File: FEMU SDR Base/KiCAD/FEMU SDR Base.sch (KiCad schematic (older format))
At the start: 11 parts

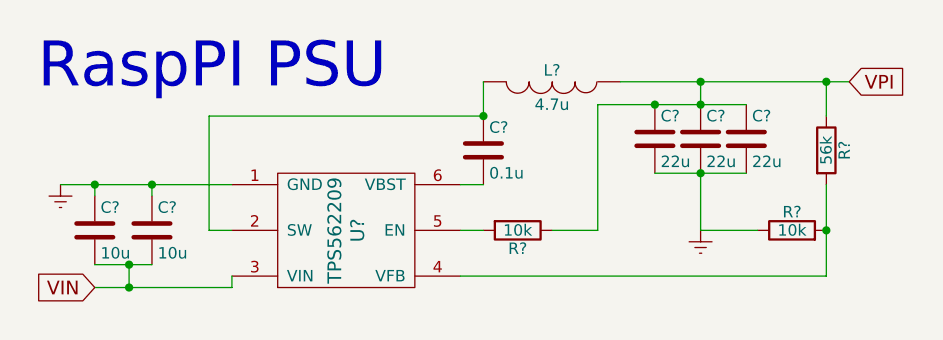
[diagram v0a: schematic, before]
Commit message: STATUS changed to FREE; Footprint ascociations added
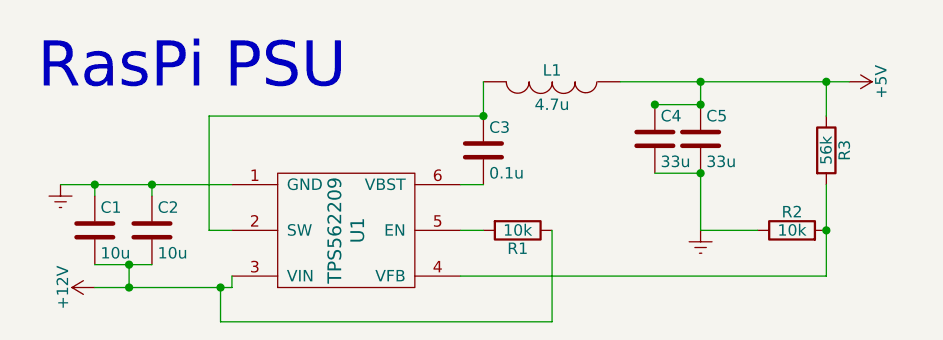
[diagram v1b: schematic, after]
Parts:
- removed C?: 22u, symbol C
- C4, C5: renamed from C?; value 22u -> 33u
- gave numbers to parts that had none: 8
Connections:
- net VIN renamed +12V
- net +12V: now also R1.1
- net VPI renamed +5V
- net +5V: no longer R1.1
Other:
- note added: "RasPi PSU"
- note removed: "RaspPI PSU"
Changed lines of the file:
@@
 LIBS:valves
 LIBS:ARB_lib
+LIBS:FEMU SDR Base-cache
 EELAYER 25 0
 EELAYER END
@@
 $EndDescr
 $Comp
-L TPS562209 U?
+L TPS562209 U1
 U 1 1 5703A8E6
 P 1800 1350
-F 0 "U?" V 1850 1350 60  0000 C CNN
+F 0 "U1" V 1850 1350 60  0000 C CNN
 F 1 "TPS562209" V 1750 1350 60  0000 C CNN
-F 2 "" H 1800 1250 60  0000 C CNN
+F 2 "" H 1800 1250 60  0001 C CNN
 F 3 "" H 1800 1250 60  0000 C CNN
 	1    1800 1350
@@
 $EndComp
 Text Notes 450  750  0    197  ~ 0
-RaspPI PSU
-$Comp
-L C C?
+RasPi PSU
+$Comp
+L C C1
 U 1 1 5703ADE8
 P 700 1350
-F 0 "C?" H 725 1450 50  0000 L CNN
+F 0 "C1" H 725 1450 50  0000 L CNN
 F 1 "10u" H 725 1250 50  0000 L CNN
-F 2 "" H 738 1200 50  0000 C CNN
+F 2 "" H 738 1200 50  0001 C CNN
 F 3 "" H 700 1350 50  0000 C CNN
 	1    700  1350
@@
 $EndComp
 $Comp
-L C C?
+L C C2
 U 1 1 5703AE4B
 P 950 1350
-F 0 "C?" H 975 1450 50  0000 L CNN
+F 0 "C2" H 975 1450 50  0000 L CNN
 F 1 "10u" H 975 1250 50  0000 L CNN
-F 2 "" H 988 1200 50  0000 C CNN
+F 2 "" H 988 1200 50  0001 C CNN
 F 3 "" H 950 1350 50  0000 C CNN
 	1    950  1350
 	1    0    0    -1
 $EndComp
-Text GLabel 700  1600 0    60   Input ~ 0
-VIN
-$Comp
-L Earth #PWR?
+$Comp
+L Earth #PWR01
 U 1 1 5703AF6B
 P 550 1150
-F 0 "#PWR?" H 550 900 50  0001 C CNN
+F 0 "#PWR01" H 550 900 50  0001 C CNN
 F 1 "Earth" H 550 1000 50  0001 C CNN
 F 2 "" H 550 1150 50  0000 C CNN
@@
 $EndComp
 $Comp
-L C C?
+L C C3
 U 1 1 5703B087
 P 2400 1000
-F 0 "C?" H 2425 1100 50  0000 L CNN
+F 0 "C3" H 2425 1100 50  0000 L CNN
 F 1 "0.1u" H 2425 900 50  0000 L CNN
-F 2 "" H 2438 850 50  0000 C CNN
+F 2 "" H 2438 850 50  0001 C CNN
 F 3 "" H 2400 1000 50  0000 C CNN
 	1    2400 1000
@@
 $EndComp
 $Comp
-L INDUCTOR L?
+L INDUCTOR L1
 U 1 1 5703B202
 P 2700 700
-F 0 "L?" V 2650 700 50  0000 C CNN
+F 0 "L1" V 2650 700 50  0000 C CNN
 F 1 "4.7u" V 2800 700 50  0000 C CNN
-F 2 "" H 2700 700 50  0000 C CNN
+F 2 "" H 2700 700 50  0001 C CNN
 F 3 "" H 2700 700 50  0000 C CNN
 	1    2700 700
@@
 $EndComp
 $Comp
-L R R?
+L R R1
 U 1 1 5703B2B6
 P 2550 1350
-F 0 "R?" V 2630 1350 50  0000 C CNN
+F 0 "R1" V 2630 1350 50  0000 C CNN
 F 1 "10k" V 2550 1350 50  0000 C CNN
-F 2 "" V 2480 1350 50  0000 C CNN
+F 2 "" V 2480 1350 50  0001 C CNN
 F 3 "" H 2550 1350 50  0000 C CNN
 	1    2550 1350
@@
 $EndComp
 $Comp
-L C C?
+L C C4
 U 1 1 5703B4E6
 P 3150 950
-F 0 "C?" H 3175 1050 50  0000 L CNN
-F 1 "22u" H 3175 850 50  0000 L CNN
-F 2 "" H 3188 800 50  0000 C CNN
+F 0 "C4" H 3175 1050 50  0000 L CNN
+F 1 "33u" H 3175 850 50  0000 L CNN
+F 2 "" H 3188 800 50  0001 C CNN
 F 3 "" H 3150 950 50  0000 C CNN
 	1    3150 950
@@
 $EndComp
 $Comp
-L C C?
+L C C5
 U 1 1 5703BAB5
 P 3350 950
-F 0 "C?" H 3375 1050 50  0000 L CNN
-F 1 "22u" H 3375 850 50  0000 L CNN
-F 2 "" H 3388 800 50  0000 C CNN
+F 0 "C5" H 3375 1050 50  0000 L CNN
+F 1 "33u" H 3375 850 50  0000 L CNN
+F 2 "" H 3388 800 50  0001 C CNN
 F 3 "" H 3350 950 50  0000 C CNN
 	1    3350 950
@@
 $EndComp
 $Comp
-L C C?
-U 1 1 5703BAE1
-P 3550 950
-F 0 "C?" H 3575 1050 50  0000 L CNN
-F 1 "22u" H 3575 850 50  0000 L CNN
-F 2 "" H 3588 800 50  0000 C CNN
-F 3 "" H 3550 950 50  0000 C CNN
-	1    3550 950
-	1    0    0    -1
-$EndComp
-Text GLabel 4000 700  2    60   Input ~ 0
-VPI
-$Comp
-L R R?
+L R R2
 U 1 1 5703C072
 P 3750 1350
-F 0 "R?" V 3830 1350 50  0000 C CNN
+F 0 "R2" V 3830 1350 50  0000 C CNN
 F 1 "10k" V 3750 1350 50  0000 C CNN
-F 2 "" V 3680 1350 50  0000 C CNN
+F 2 "" V 3680 1350 50  0001 C CNN
 F 3 "" H 3750 1350 50  0000 C CNN
 	1    3750 1350
@@
 $EndComp
 $Comp
-L R R?
+L R R3
 U 1 1 5703C16C
 P 3900 1000
-F 0 "R?" V 3980 1000 50  0000 C CNN
+F 0 "R3" V 3980 1000 50  0000 C CNN
 F 1 "56k" V 3900 1000 50  0000 C CNN
-F 2 "" V 3830 1000 50  0000 C CNN
+F 2 "" V 3830 1000 50  0001 C CNN
 F 3 "" H 3900 1000 50  0000 C CNN
 	1    3900 1000
@@
 $EndComp
 $Comp
-L Earth #PWR?
+L Earth #PWR02
 U 1 1 5703C400
 P 3350 1350
-F 0 "#PWR?" H 3350 1100 50  0001 C CNN
+F 0 "#PWR02" H 3350 1100 50  0001 C CNN
 F 1 "Earth" H 3350 1200 50  0001 C CNN
 F 2 "" H 3350 1350 50  0000 C CNN
@@
 Wire Wire Line
 	2400 850  2400 700
-Wire Wire Line
-	2400 1350 2300 1350
-Wire Wire Line
-	2900 800  3550 800
 Connection ~ 3350 800
 Wire Wire Line
 	3350 700  3350 800
-Wire Wire Line
-	2900 800  2900 1350
-Wire Wire Line
-	2900 1350 2700 1350
 Connection ~ 3150 800
 Connection ~ 3350 700
@@
 	3900 1550 2300 1550
 Connection ~ 3900 1350
-Wire Wire Line
-	3150 1100 3550 1100
 Connection ~ 3350 1100
 Wire Wire Line
@@
 Wire Wire Line
 	3350 1350 3600 1350
+Wire Wire Line
+	2400 1350 2300 1350
+Wire Wire Line
+	2700 1350 2700 1750
+Wire Wire Line
+	2700 1750 1250 1750
+Wire Wire Line
+	1250 1750 1250 1600
+Connection ~ 1250 1600
+Wire Wire Line
+	3350 800  3150 800
+Wire Wire Line
+	3350 1100 3150 1100
+$Comp
+L +12V #PWR03
+U 1 1 57077D61
+P 700 1600
+F 0 "#PWR03" H 700 1450 50  0001 C CNN
+F 1 "+12V" H 700 1740 50  0000 C CNN
+F 2 "" H 700 1600 50  0000 C CNN
+F 3 "" H 700 1600 50  0000 C CNN
+	1    700  1600
+	0    -1   -1   0
+$EndComp
+$Comp
+L +5V #PWR04
+U 1 1 57077E13
+P 4000 700
+F 0 "#PWR04" H 4000 550 50  0001 C CNN
+F 1 "+5V" H 4000 840 50  0000 C CNN
+F 2 "" H 4000 700 50  0000 C CNN
+F 3 "" H 4000 700 50  0000 C CNN
+	1    4000 700
+	0    1    1    0
+$EndComp
 $EndSCHEMATC

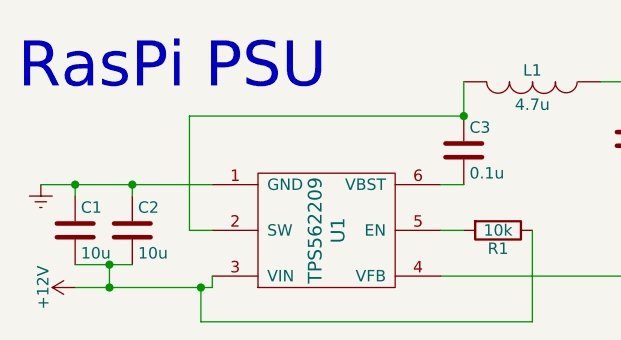
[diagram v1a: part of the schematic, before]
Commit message: STATUS = FREE ; pcbnew layout of RasPi PSU added, Changed to 4 layers.
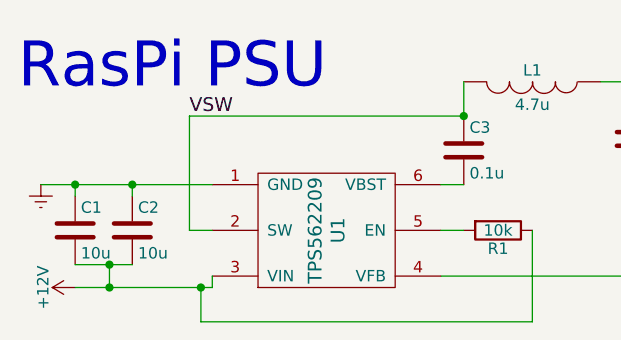
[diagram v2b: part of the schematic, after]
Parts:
- C1, C2, C3: footprint (none) -> Capacitors_SMD:C_0805_HandSoldering
- C4, C5: footprint (none) -> Capacitors_SMD:C_1206_HandSoldering
- L1: footprint (none) -> ARB_foots:L_Wurth_74404052039
- R1, R2, R3: footprint (none) -> Resistors_SMD:R_0805_HandSoldering
- U1: footprint (none) -> ARB_foots:TPS562209
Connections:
- net VSW: now reaches C3.1, L1.2, U1.2 (SW)
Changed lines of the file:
@@
 F 0 "U1" V 1850 1350 60  0000 C CNN
 F 1 "TPS562209" V 1750 1350 60  0000 C CNN
-F 2 "" H 1800 1250 60  0001 C CNN
+F 2 "ARB_foots:TPS562209" H 1800 1250 60  0001 C CNN
 F 3 "" H 1800 1250 60  0000 C CNN
 	1    1800 1350
@@
 F 0 "C1" H 725 1450 50  0000 L CNN
 F 1 "10u" H 725 1250 50  0000 L CNN
-F 2 "" H 738 1200 50  0001 C CNN
+F 2 "Capacitors_SMD:C_0805_HandSoldering" H 738 1200 50  0001 C CNN
 F 3 "" H 700 1350 50  0000 C CNN
 	1    700  1350
@@
 F 0 "C2" H 975 1450 50  0000 L CNN
 F 1 "10u" H 975 1250 50  0000 L CNN
-F 2 "" H 988 1200 50  0001 C CNN
+F 2 "Capacitors_SMD:C_0805_HandSoldering" H 988 1200 50  0001 C CNN
 F 3 "" H 950 1350 50  0000 C CNN
 	1    950  1350
@@
 F 0 "C3" H 2425 1100 50  0000 L CNN
 F 1 "0.1u" H 2425 900 50  0000 L CNN
-F 2 "" H 2438 850 50  0001 C CNN
+F 2 "Capacitors_SMD:C_0805_HandSoldering" H 2438 850 50  0001 C CNN
 F 3 "" H 2400 1000 50  0000 C CNN
 	1    2400 1000
@@
 F 0 "L1" V 2650 700 50  0000 C CNN
 F 1 "4.7u" V 2800 700 50  0000 C CNN
-F 2 "" H 2700 700 50  0001 C CNN
+F 2 "ARB_foots:L_Wurth_74404052039" H 2700 700 50  0001 C CNN
 F 3 "" H 2700 700 50  0000 C CNN
 	1    2700 700
@@
 F 0 "R1" V 2630 1350 50  0000 C CNN
 F 1 "10k" V 2550 1350 50  0000 C CNN
-F 2 "" V 2480 1350 50  0001 C CNN
+F 2 "Resistors_SMD:R_0805_HandSoldering" V 2480 1350 50  0001 C CNN
 F 3 "" H 2550 1350 50  0000 C CNN
 	1    2550 1350
@@
 F 0 "C4" H 3175 1050 50  0000 L CNN
 F 1 "33u" H 3175 850 50  0000 L CNN
-F 2 "" H 3188 800 50  0001 C CNN
+F 2 "Capacitors_SMD:C_1206_HandSoldering" H 3188 800 50  0001 C CNN
 F 3 "" H 3150 950 50  0000 C CNN
 	1    3150 950
@@
 F 0 "C5" H 3375 1050 50  0000 L CNN
 F 1 "33u" H 3375 850 50  0000 L CNN
-F 2 "" H 3388 800 50  0001 C CNN
+F 2 "Capacitors_SMD:C_1206_HandSoldering" H 3388 800 50  0001 C CNN
 F 3 "" H 3350 950 50  0000 C CNN
 	1    3350 950
@@
 F 0 "R2" V 3830 1350 50  0000 C CNN
 F 1 "10k" V 3750 1350 50  0000 C CNN
-F 2 "" V 3680 1350 50  0001 C CNN
+F 2 "Resistors_SMD:R_0805_HandSoldering" V 3680 1350 50  0001 C CNN
 F 3 "" H 3750 1350 50  0000 C CNN
 	1    3750 1350
@@
 F 0 "R3" V 3980 1000 50  0000 C CNN
 F 1 "56k" V 3900 1000 50  0000 C CNN
-F 2 "" V 3830 1000 50  0001 C CNN
+F 2 "Resistors_SMD:R_0805_HandSoldering" V 3830 1000 50  0001 C CNN
 F 3 "" H 3900 1000 50  0000 C CNN
 	1    3900 1000
@@
 	0    1    1    0
 $EndComp
+Text Label 1200 850  0    60   ~ 0
+VSW
 $EndSCHEMATC

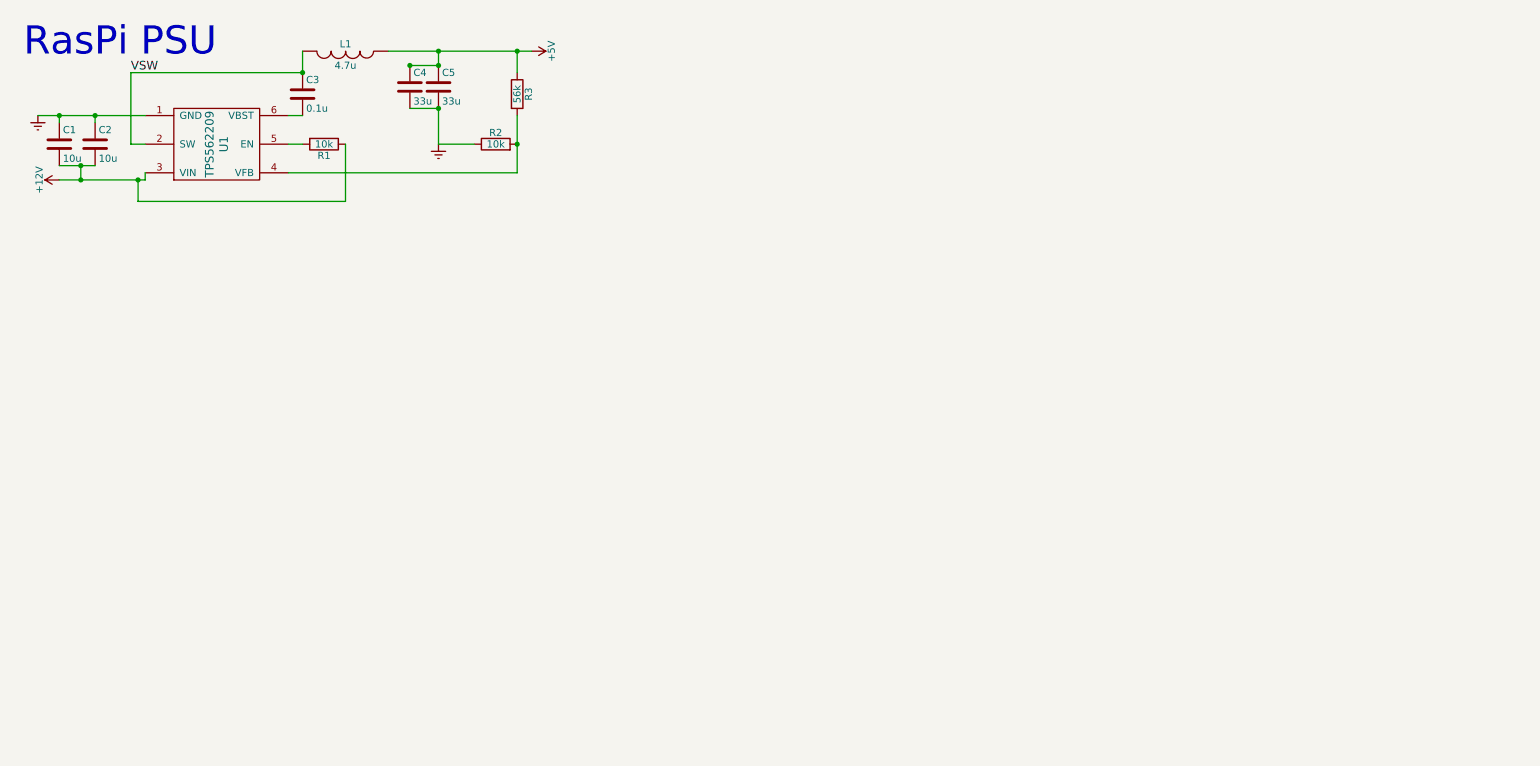
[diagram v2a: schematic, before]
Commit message: Started populating schematic
Signed-off-by: hardiepienaar <hardiepienaar@gmail.com>
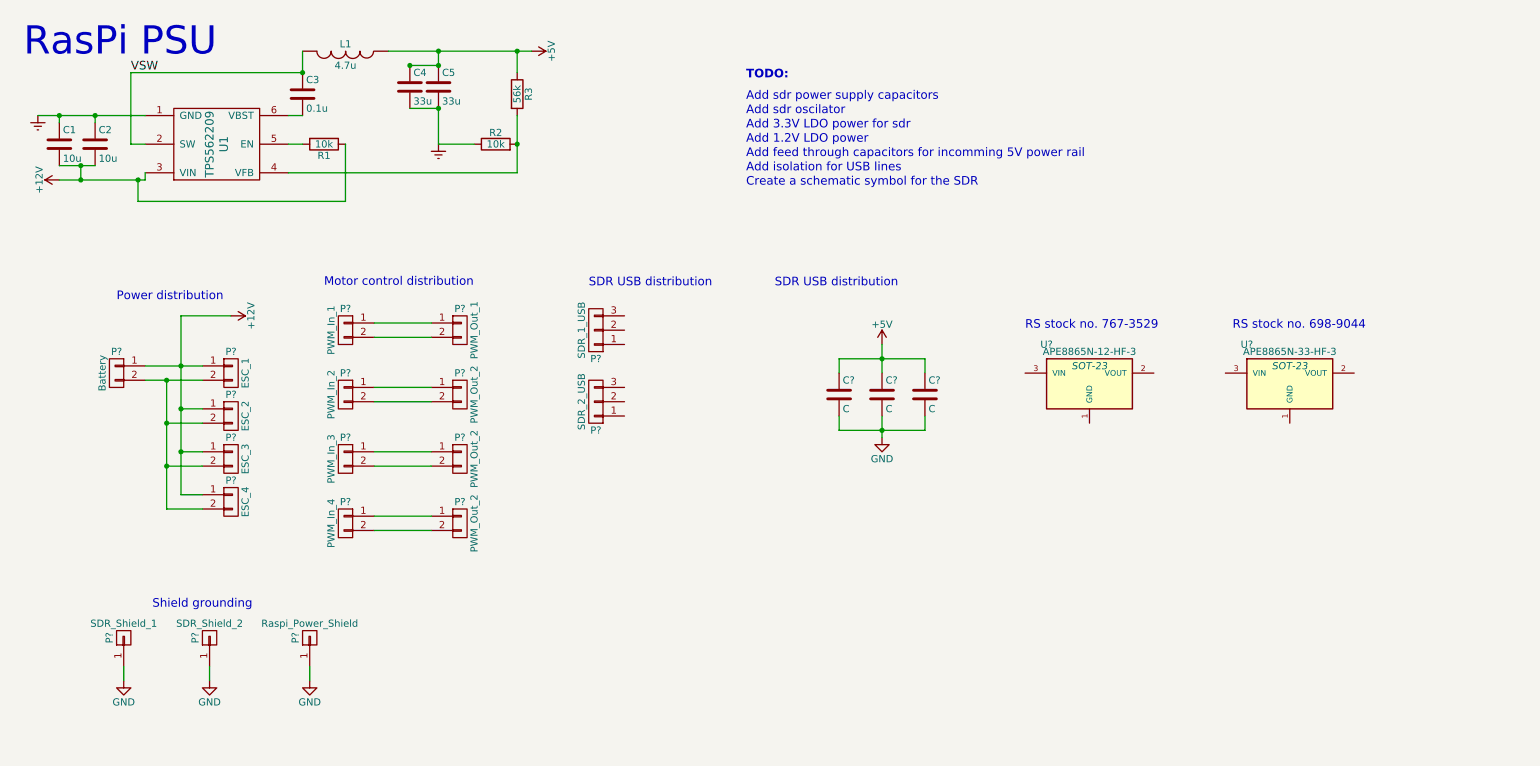
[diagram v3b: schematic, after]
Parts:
- added C? (x3): C, symbol C
- added P?: Battery, symbol CONN_01X02
- added P?: ESC_1, symbol CONN_01X02
- added P?: ESC_2, symbol CONN_01X02
- added P?: ESC_3, symbol CONN_01X02
- added P?: ESC_4, symbol CONN_01X02
- added P?: PWM_In_1, symbol CONN_01X02
- added P?: PWM_In_2, symbol CONN_01X02
- added P?: PWM_In_3, symbol CONN_01X02
- added P?: PWM_In_4, symbol CONN_01X02
- added P?: PWM_Out_1, symbol CONN_01X02
- added P? (x3): PWM_Out_2, symbol CONN_01X02
- added P?: SDR_Shield_1, symbol CONN_01X01
- added P?: SDR_Shield_2, symbol CONN_01X01
- added P?: Raspi_Power_Shield, symbol CONN_01X01
- added P?: SDR_1_USB, symbol CONN_01X03
- added P?: SDR_2_USB, symbol CONN_01X03
- added U?: APE8865N-12-HF-3, SOT-23, symbol APE8865N-12-HF-3
- added U?: APE8865N-33-HF-3, SOT-23, symbol APE8865N-33-HF-3
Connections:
- net +12V: now also P?.1 (P1), P?.1 (P1), P?.1 (P1), P?.1 (P1), P?.1 (P1)
- net +5V: now also C?.1, C?.1, C?.1
- new net: P?.2 (P2), P?.2 (P2), P?.2 (P2), P?.2 (P2), P?.2 (P2)
- new net: P?.1 (P1), P?.1 (P1) (x4)
- new net: P?.2 (P2), P?.2 (P2) (x4)
- new net GND: C?.2, C?.2, C?.2, P?.1 (P1), P?.1 (P1), P?.1 (P1)
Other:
- note added: "Add 1.2V LDO power"
- note added: "Add 3.3V LDO power for sdr\n"
- note added: "Add feed through capacitors for incomming 5V power rail"
- note added: "Add isolation for USB lines\n"
- note added: "Add sdr oscilator"
- note added: "Add sdr power supply capacitors\n"
- note added: "Create a schematic symbol for the SDR"
- note added: "Motor control distribution\n"
- note added: "Power distribution\n"
- note added: "RS stock no. 698-9044"
- note added: "RS stock no. 767-3529"
- note added: "SDR USB distribution\n\n"
- note added: "Shield grounding\n"
- note added: "TODO:"

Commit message: added footprints and some elements to netlist
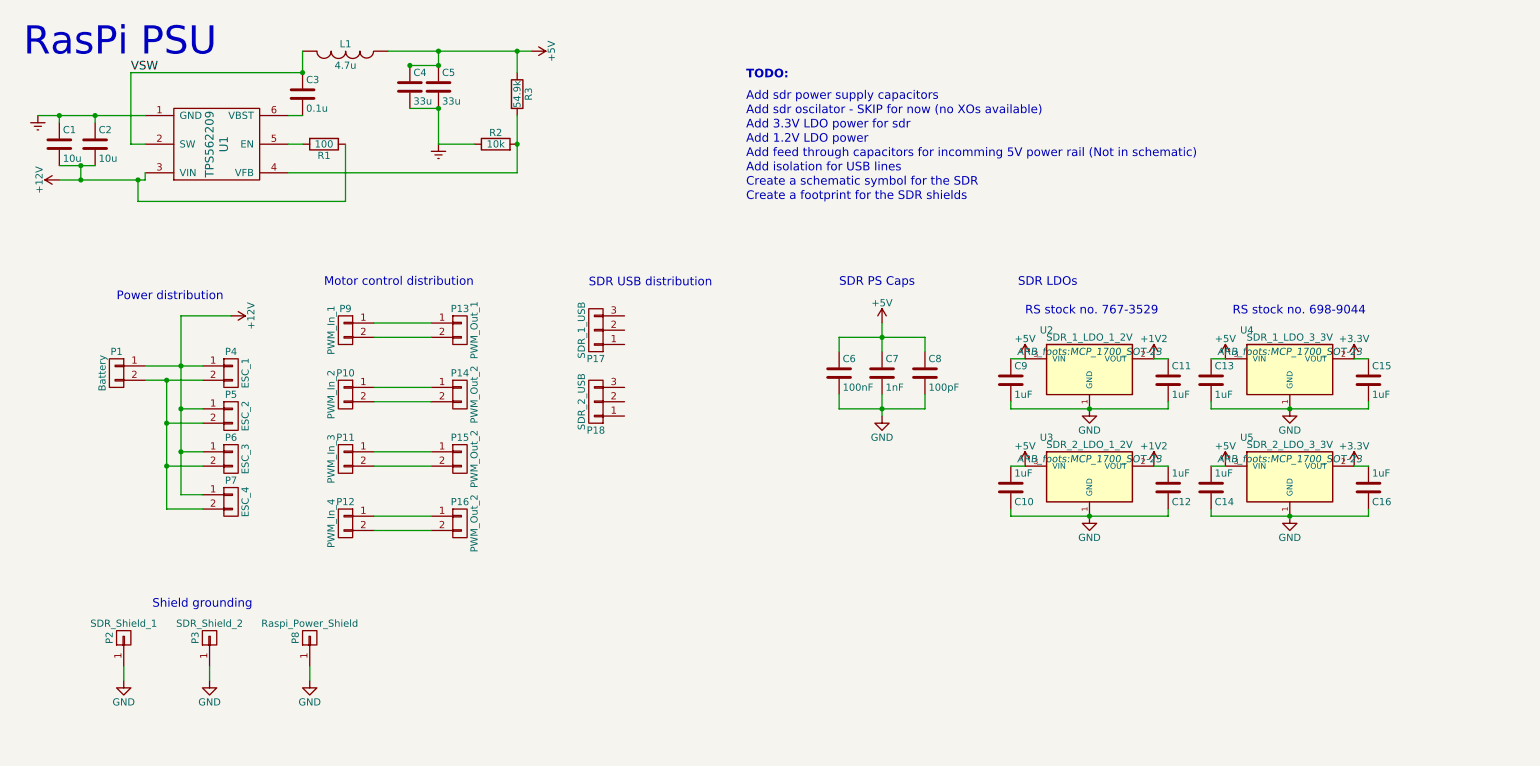
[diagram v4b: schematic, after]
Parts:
- added C10, C11, C12, C13, C14, C15, C16, C9: 1uF, Capacitors_SMD:C_0805_HandSoldering, symbol C
- added U3: SDR_2_LDO_1_2V, ARB_foots:MCP_1700_SOT-23, symbol APE8865N-12-HF-3
- added U5: SDR_2_LDO_3_3V, ARB_foots:MCP_1700_SOT-23, symbol APE8865N-33-HF-3
- C6: renamed from C?; value C -> 100nF; footprint (none) -> Capacitors_SMD:C_0805_HandSoldering
- C7: renamed from C?; value C -> 1nF; footprint (none) -> Capacitors_SMD:C_0805_HandSoldering
- C8: renamed from C?; value C -> 100pF; footprint (none) -> Capacitors_SMD:C_0805_HandSoldering
- P8: renamed from P?; footprint (none) -> ARB_foots:PCB_Shield_29x25mm
- R1: value 10k -> 100
- R3: value 56k -> 54.9k
- U2: renamed from U?; value APE8865N-12-HF-3 -> SDR_1_LDO_1_2V; footprint SOT-23 -> ARB_foots:MCP_1700_SOT-23
- U4: renamed from U?; value APE8865N-33-HF-3 -> SDR_1_LDO_3_3V; footprint SOT-23 -> ARB_foots:MCP_1700_SOT-23
- gave numbers to parts that had none: 17
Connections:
- net +5V: now also U2.3 (VIN), U4.3 (VIN), C10.2, C13.1, C14.2, C9.1, U3.3 (VIN), U5.3 (VIN)
- net GND: now also U2.1 (GND), U4.1 (GND), C10.1, C11.2, C12.1, C13.2, C14.1, C15.2, C16.1, C9.2, U3.1 (GND), U5.1 (GND)
- net +1V2: now reaches U2.2 (VOUT)
- net +1V2: now also C11.1, C12.2, U3.2 (VOUT)
- net +3V3: now reaches U4.2 (VOUT)
- net +3V3: now also C15.1, C16.2, U5.2 (VOUT)
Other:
- note added: "Add feed through capacitors for incomming 5V power rail (Not in schematic)"
- note added: "Add sdr oscilator - SKIP for now (no XOs available)"
- note added: "Create a footprint for the SDR shields"
- note added: "SDR LDOs"
- note added: "SDR PS Caps"
- note removed: "Add feed through capacitors for incomming 5V power rail"
- note removed: "Add sdr oscilator"
- moved on the sheet: C6, C7, C8, U2, U4
